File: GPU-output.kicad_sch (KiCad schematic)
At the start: 20 parts, among them J1 Conn_1-2212115-4, Q1 2N7002K-T1-E3, U4 TMCS1100A2-Q1

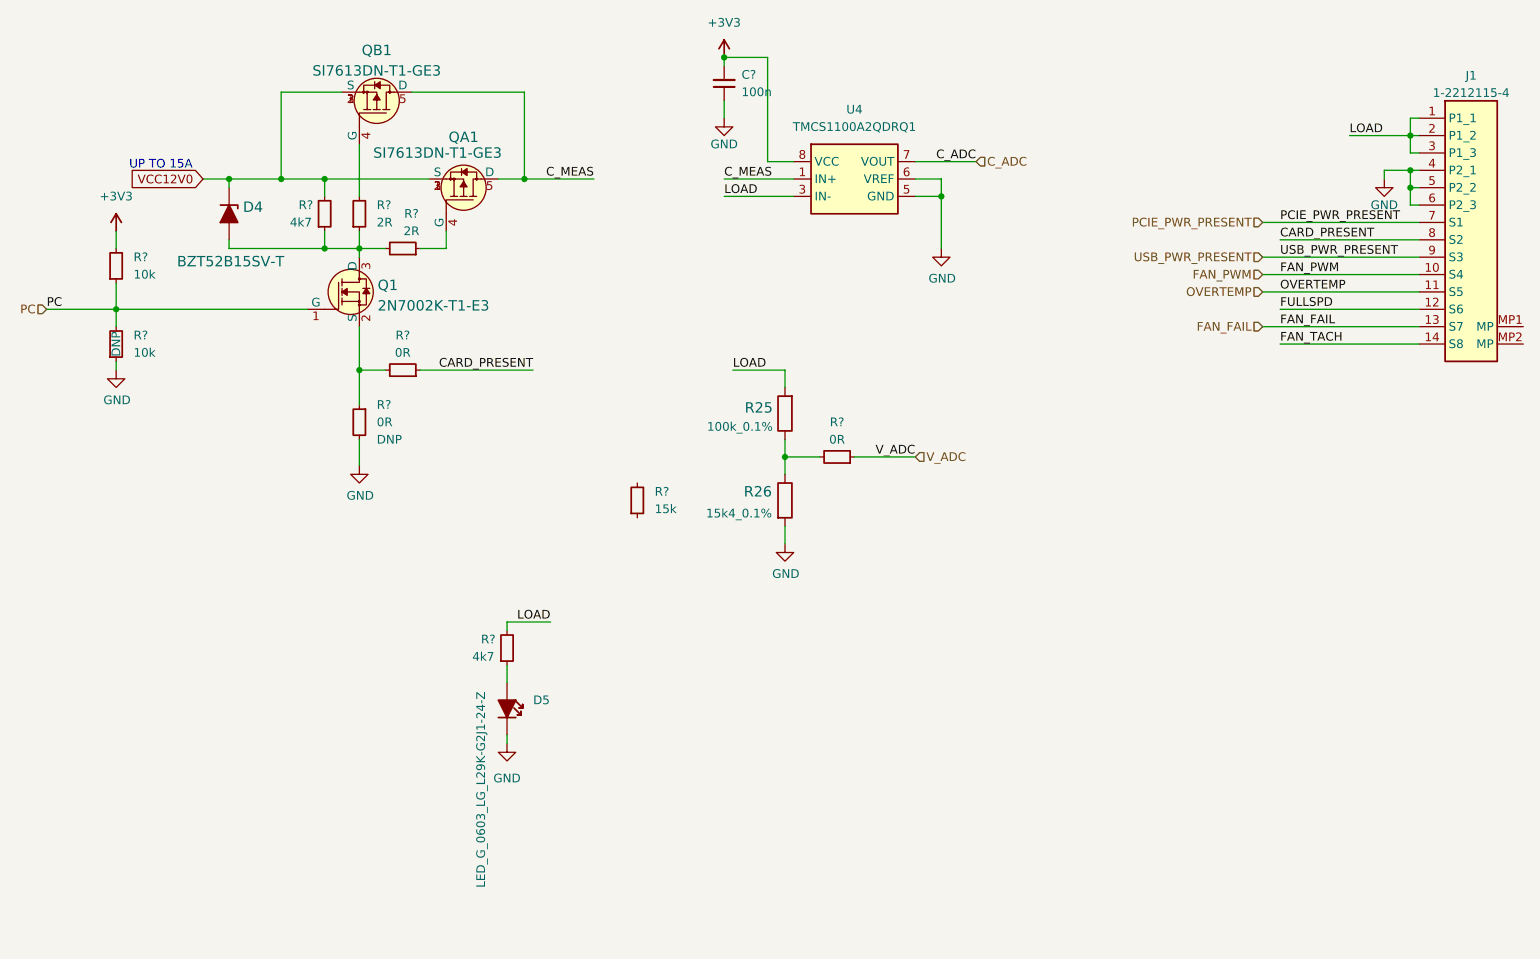
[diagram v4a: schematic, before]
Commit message: Standarize debug signal schematic
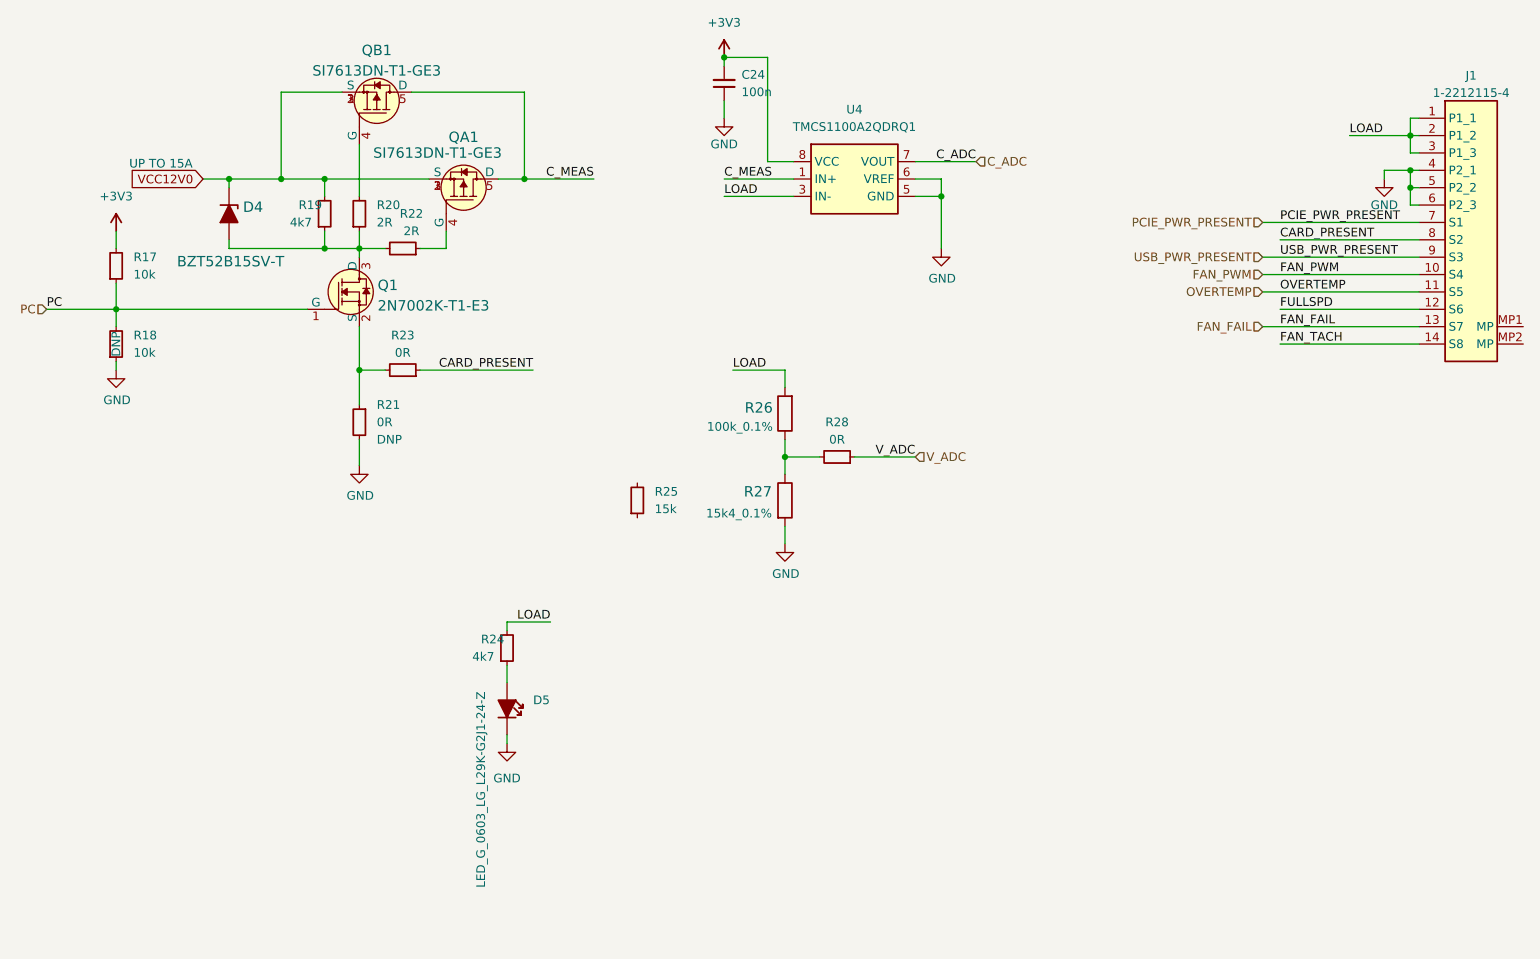
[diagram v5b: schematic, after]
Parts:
- gave numbers to parts that had none: 11
- renumbered R25 to R26, R26 to R27
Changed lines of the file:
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@@
   (symbol (lib_id "antmicroResistors0402:R_100k_0.1%_0402") (at 140.97 87.63 90) (unit 1)
     (in_bom yes) (on_board yes) (fields_autoplaced)
-    (property "Reference" "R25" (id 0) (at 139.1921 86.7954 90)
+    (property "Reference" "R26" (id 0) (at 139.1921 86.7954 90)
       (effects (font (size 1.524 1.524)) (justify left))
     )
@@
   (symbol (lib_name "R_0R_0402_1") (lib_id "antmicroResistors0402:R_0R_0402") (at 87.63 81.28 180) (unit 1)
     (in_bom yes) (on_board yes)
-    (property "Reference" "R?" (id 0) (at 85.09 76.2 0)
+    (property "Reference" "R23" (id 0) (at 85.09 76.2 0)
       (effects (font (size 1.27 1.27) (thickness 0.15)))
     )
@@
   (symbol (lib_name "R_4k7_0402_1") (lib_id "antmicroResistors0402:R_4k7_0402") (at 100.33 124.46 90) (unit 1)
     (in_bom yes) (on_board yes)
-    (property "Reference" "R?" (id 0) (at 96.52 120.65 90)
+    (property "Reference" "R24" (id 0) (at 96.52 120.65 90)
       (effects (font (size 1.27 1.27) (thickness 0.15)) (justify right))
     )
@@
   (symbol (lib_id "antmicroResistors0402:R_15k4_0.1%_0402") (at 140.97 100.33 270) (unit 1)
     (in_bom yes) (on_board yes)
-    (property "Reference" "R26" (id 0) (at 139.065 99.0601 90)
+    (property "Reference" "R27" (id 0) (at 139.065 99.0601 90)
       (effects (font (size 1.524 1.524)) (justify right))
     )
@@
   (symbol (lib_name "R_10k_0402_1") (lib_id "antmicroResistors0402:R_10k_0402") (at 43.18 68.58 90) (unit 1)
     (in_bom yes) (on_board yes) (fields_autoplaced)
-    (property "Reference" "R?" (id 0) (at 45.72 64.7699 90)
+    (property "Reference" "R17" (id 0) (at 45.72 64.7699 90)
       (effects (font (size 1.27 1.27) (thickness 0.15)) (justify right))
     )
@@
   (symbol (lib_name "R_4k7_0402_1") (lib_id "antmicroResistors0402:R_4k7_0402") (at 73.66 60.96 90) (unit 1)
     (in_bom yes) (on_board yes)
-    (property "Reference" "R?" (id 0) (at 69.85 57.15 90)
+    (property "Reference" "R19" (id 0) (at 69.85 57.15 90)
       (effects (font (size 1.27 1.27) (thickness 0.15)) (justify right))
     )
@@
   (symbol (lib_name "R_0R_0402_1") (lib_id "antmicroResistors0402:R_0R_0402") (at 151.13 93.98 180) (unit 1)
     (in_bom yes) (on_board yes)
-    (property "Reference" "R?" (id 0) (at 148.59 88.9 0)
+    (property "Reference" "R28" (id 0) (at 148.59 88.9 0)
       (effects (font (size 1.27 1.27) (thickness 0.15)))
     )
@@
   (symbol (lib_name "R_10k_0402_1") (lib_id "antmicroResistors0402:R_10k_0402") (at 43.18 80.01 90) (unit 1)
     (in_bom yes) (on_board yes)
-    (property "Reference" "R?" (id 0) (at 45.72 76.1999 90)
+    (property "Reference" "R18" (id 0) (at 45.72 76.1999 90)
       (effects (font (size 1.27 1.27) (thickness 0.15)) (justify right))
     )
@@
   (symbol (lib_id "antmicroResistors0402:R_15k_0.1%_0402") (at 119.38 102.87 90) (unit 1)
     (in_bom yes) (on_board yes) (fields_autoplaced)
-    (property "Reference" "R?" (id 0) (at 121.92 99.0599 90)
+    (property "Reference" "R25" (id 0) (at 121.92 99.0599 90)
       (effects (font (size 1.27 1.27) (thickness 0.15)) (justify right))
     )
@@
   (symbol (lib_name "R_2R_0402_1") (lib_id "antmicroResistors0402:R_2R_0402") (at 87.63 63.5 180) (unit 1)
     (in_bom yes) (on_board yes)
-    (property "Reference" "R?" (id 0) (at 86.36 58.42 0)
+    (property "Reference" "R22" (id 0) (at 86.36 58.42 0)
       (effects (font (size 1.27 1.27) (thickness 0.15)))
     )
@@
   (symbol (lib_name "R_2R_0402_1") (lib_id "antmicroResistors0402:R_2R_0402") (at 78.74 60.96 90) (unit 1)
     (in_bom yes) (on_board yes) (fields_autoplaced)
-    (property "Reference" "R?" (id 0) (at 81.28 57.1499 90)
+    (property "Reference" "R20" (id 0) (at 81.28 57.1499 90)
       (effects (font (size 1.27 1.27) (thickness 0.15)) (justify right))
     )
@@
   (symbol (lib_name "R_0R_0402_1") (lib_id "antmicroResistors0402:R_0R_0402") (at 78.74 86.36 270) (unit 1)
     (in_bom yes) (on_board yes) (fields_autoplaced)
-    (property "Reference" "R?" (id 0) (at 81.28 86.3599 90)
+    (property "Reference" "R21" (id 0) (at 81.28 86.3599 90)
       (effects (font (size 1.27 1.27) (thickness 0.15)) (justify left))
     )
@@
   (symbol (lib_name "C_100n_0402_1") (lib_id "antmicroCapacitors0402:C_100n_0402") (at 132.08 41.91 90) (unit 1)
     (in_bom yes) (on_board yes) (fields_autoplaced)
-    (property "Reference" "C?" (id 0) (at 134.62 38.0935 90)
-      (effects (font (size 1.27 1.27) (thickness 0.15)) (justify right))
-    )
+    (property "Reference" "C24" (id 0) (at 134.62 38.0935 90)
+      (effects (font (size 1.27 1.27) (thickness 0.15)) (justify right))
+    )

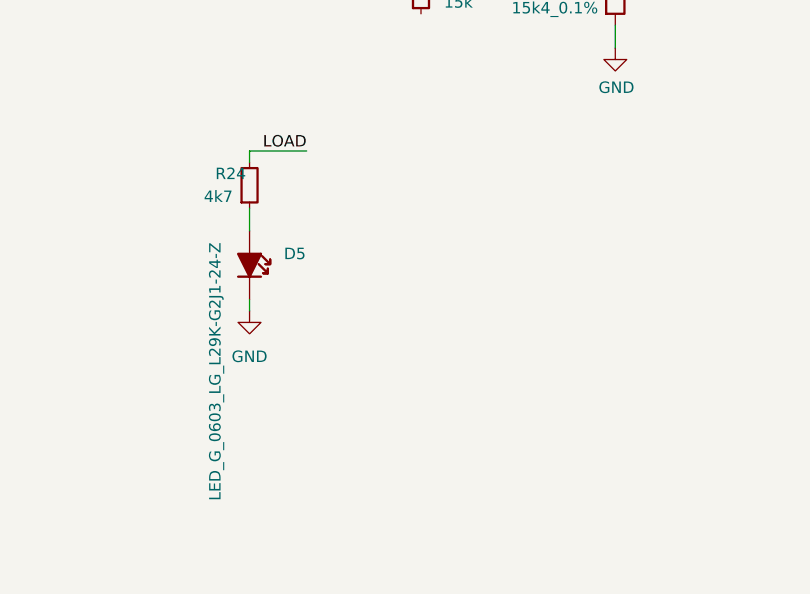
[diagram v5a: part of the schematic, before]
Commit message: Standarize missing components
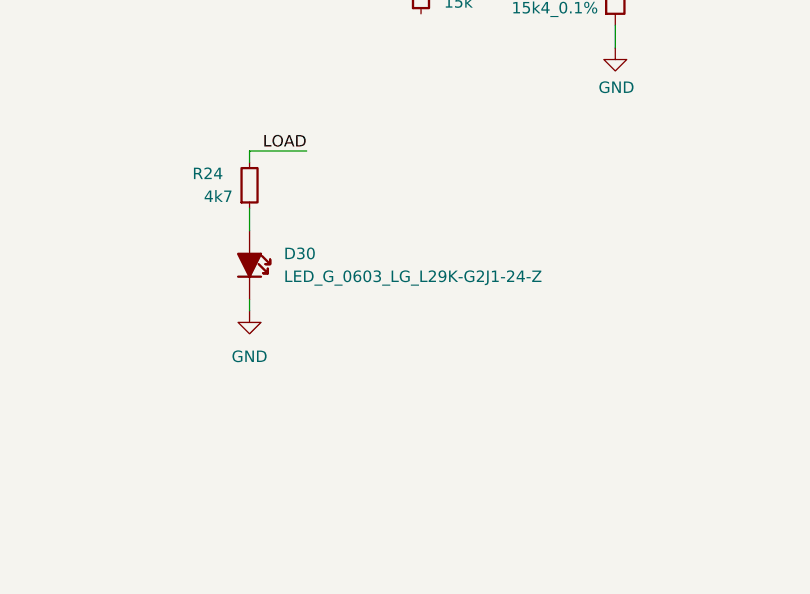
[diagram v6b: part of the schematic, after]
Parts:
- removed D5: LED_G_0603_LG_L29K-G2J1-24-Z, antmicro-footprints:LED_0603_1608Metric_G, symbol antmicroLEDIndicationDiscrete:LED_G_0603_LG_L29K-G2J1-24-Z
- added D30: LED_G_0603_LG_L29K-G2J1-24-Z, antmicro-footprints:LED_0603_1608Metric_G, symbol antmicroLEDIndicationDiscrete:LED_G_0603_LG_L29K-G2J1-24-Z
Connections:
- net GND: now also D30.2
- net at R24.1: now also D30.1
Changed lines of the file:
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@@
   (symbol (lib_name "R_4k7_0402_1") (lib_id "antmicroResistors0402:R_4k7_0402") (at 100.33 124.46 90) (unit 1)
     (in_bom yes) (on_board yes)
-    (property "Reference" "R24" (id 0) (at 96.52 120.65 90)
+    (property "Reference" "R24" (id 0) (at 93.98 120.65 90)
       (effects (font (size 1.27 1.27) (thickness 0.15)) (justify right))
     )
@@
     (pin "2")
   )
+  (symbol (lib_id "antmicroLEDIndicationDiscrete:LED_G_0603_LG_L29K-G2J1-24-Z") (at 100.33 127 270) (unit 1)
+    (in_bom yes) (on_board yes) (fields_autoplaced)
+    (property "Reference" "D30" (id 0) (at 104.14 129.5399 90)
+      (effects (font (size 1.27 1.27) (thickness 0.15)) (justify left))
+    )
+    (property "Value" "LED_G_0603_LG_L29K-G2J1-24-Z" (id 1) (at 104.14 132.0799 90)
+      (effects (font (size 1.27 1.27) (thickness 0.15)) (justify left))
+    )
+    (property "Footprint" "antmicro-footprints:LED_0603_1608Metric_G" (id 2) (at 90.17 149.86 0)
+      (effects (font (size 1.27 1.27) (thickness 0.15)) (justify left bottom) hide)
+    )
+    (property "Datasheet" "https://dammedia.osram.info/media/resource/hires/osram-dam-2493945/LG%20L29K.pdf" (id 3) (at 87.63 149.86 0)
+      (effects (font (size 1.27 1.27) (thickness 0.15)) (justify left bottom) hide)
+    )
+    (property "MPN" "LG L29K-G2J1-24-Z" (id 4) (at 85.09 149.86 0)
+      (effects (font (size 1.27 1.27) (thickness 0.15)) (justify left bottom) hide)
+    )
+    (property "Manufacturer" "OSRAM" (id 5) (at 82.55 149.86 0)
+      (effects (font (size 1.27 1.27) (thickness 0.15)) (justify left bottom) hide)
+    )
+    (property "Author" "Antmicro" (id 6) (at 80.01 149.86 0)
+      (effects (font (size 1.27 1.27) (thickness 0.15)) (justify left bottom) hide)
+    )
+    (property "License" "Apache-2.0" (id 7) (at 77.47 149.86 0)
+      (effects (font (size 1.27 1.27) (thickness 0.15)) (justify left bottom) hide)
+    )
+    (pin "1")
+    (pin "2")
+  )
   (symbol (lib_id "antmicropower:GND") (at 100.33 135.89 0) (unit 1)
     (in_bom yes) (on_board yes) (fields_autoplaced)
@@
     (pin "1")
   )
-  (symbol (lib_id "antmicroLEDIndicationDiscrete:LED_G_0603_LG_L29K-G2J1-24-Z") (at 100.33 127 270) (unit 1)
-    (in_bom yes) (on_board yes)
-    (property "Reference" "D5" (id 0) (at 104.14 129.5399 90)
-      (effects (font (size 1.27 1.27) (thickness 0.15)) (justify left))
-    )
-    (property "Value" "LED_G_0603_LG_L29K-G2J1-24-Z" (id 1) (at 96.52 128.27 0)
-      (effects (font (size 1.27 1.27) (thickness 0.15)) (justify left))
-    )
-    (property "Footprint" "antmicro-footprints:LED_0603_1608Metric_G" (id 2) (at 90.17 149.86 0)
-      (effects (font (size 1.27 1.27) (thickness 0.15)) (justify left bottom) hide)
-    )
-    (property "Datasheet" "https://dammedia.osram.info/media/resource/hires/osram-dam-2493945/LG%20L29K.pdf" (id 3) (at 87.63 149.86 0)
-      (effects (font (size 1.27 1.27) (thickness 0.15)) (justify left bottom) hide)
-    )
-    (property "MPN" "LG L29K-G2J1-24-Z" (id 4) (at 85.09 149.86 0)
-      (effects (font (size 1.27 1.27) (thickness 0.15)) (justify left bottom) hide)
-    )
-    (property "Manufacturer" "OSRAM" (id 5) (at 82.55 149.86 0)
-      (effects (font (size 1.27 1.27) (thickness 0.15)) (justify left bottom) hide)
-    )
-    (property "Author" "Antmicro" (id 6) (at 80.01 149.86 0)
-      (effects (font (size 1.27 1.27) (thickness 0.15)) (justify left bottom) hide)
-    )
-    (property "License" "Apache-2.0" (id 7) (at 77.47 149.86 0)
-      (effects (font (size 1.27 1.27) (thickness 0.15)) (justify left bottom) hide)
-    )
-    (pin "1")
-    (pin "2")
-  )
   (symbol (lib_id "antmicroPowerMeasurement:TMCS1100A2-Q1") (at 142.24 50.8 0) (unit 1)

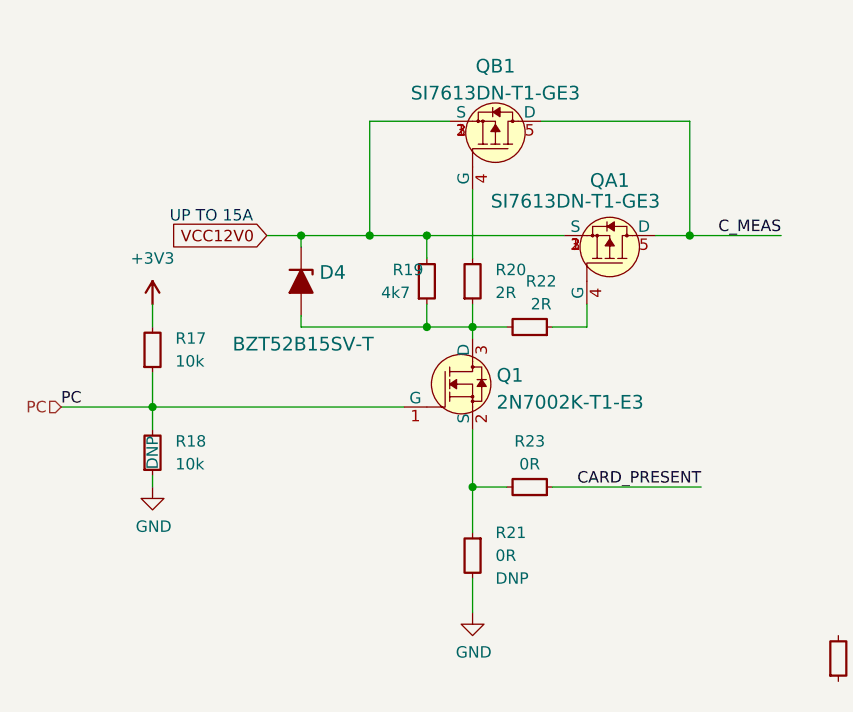
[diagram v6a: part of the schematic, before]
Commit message: 2nd batch of standardization of schematic
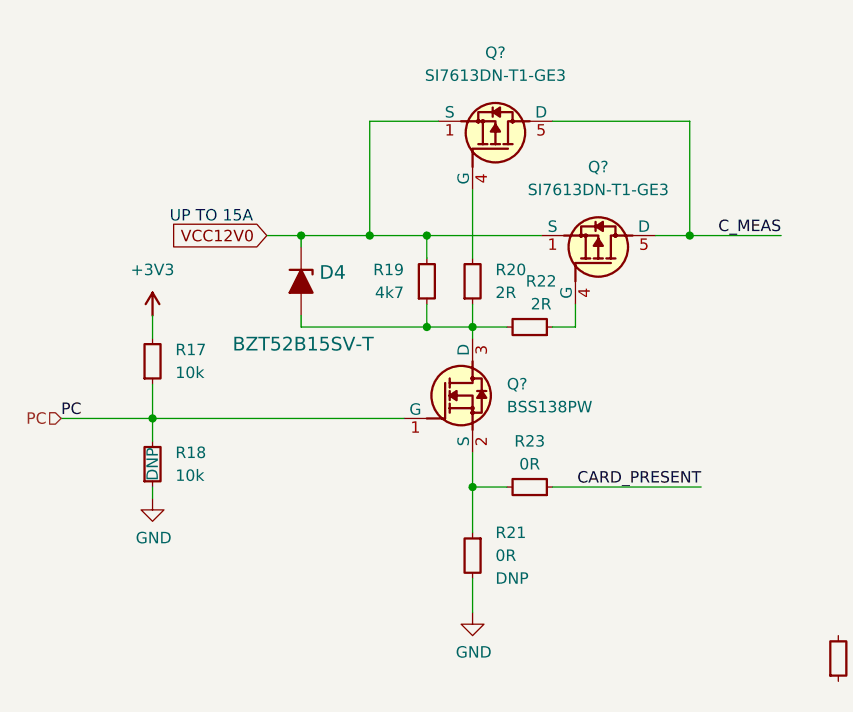
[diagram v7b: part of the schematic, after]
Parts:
- removed Q1: 2N7002K-T1-E3, antmicro-footprints:SOT-23-3, symbol antmicroTransistorsFETsMOSFETsSingle:2N7002K-T1-E3
- removed QA1, QB1: SI7613DN-T1-GE3, antmicro-footprints:Vishay_PowerPAK_1212-8_Single, symbol antmicroTransistorsFETsMOSFETsSingle:SI7613DN-T1-GE3
- added Q? (x2): SI7613DN-T1-GE3, antmicro-footprints:Vishay_PowerPAK_1212-8_Single, symbol antmicroTransistorsFETsMOSFETsSingle:SI7613DN-T1-GE3
- added Q?: BSS138PW, antmicro-footprints:SC70-3, symbol antmicroTransistorsFETsMOSFETsSingle:BSS138PW
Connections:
- net C_MEAS: now also Q?.5 (D), Q?.5 (D)
- net PC: now also Q?.1 (G)
- net VCC12V0: now also Q?.1 (S), Q?.1 (S), Q?.2 (S), Q?.2 (S), Q?.3 (S), Q?.3 (S)
- net at R21.1, R23.2: now also Q?.2 (S)
- net at D4.A, R19.1, R20.1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: now also Q?.3 (D)
- net at R22.1: now also Q?.4 (G)
- net at R20.2: now also Q?.4 (G)
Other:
- moved on the sheet: R17, R18

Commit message: Next batch of standardization
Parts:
- gave numbers to parts that had none: 3
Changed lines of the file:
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@@
   (symbol (lib_name "SI7613DN-T1-GE3_1") (lib_id "antmicroTransistorsFETsMOSFETsSingle:SI7613DN-T1-GE3") (at 78.74 48.26 270) (mirror x) (unit 1)
     (in_bom yes) (on_board yes) (fields_autoplaced)
-    (property "Reference" "Q?" (id 0) (at 81.28 33.02 90)
+    (property "Reference" "Q2" (id 0) (at 81.28 33.02 90)
       (effects (font (size 1.27 1.27) (thickness 0.15)))
     )
@@
   (symbol (lib_name "SI7613DN-T1-GE3_1") (lib_id "antmicroTransistorsFETsMOSFETsSingle:SI7613DN-T1-GE3") (at 90.17 60.96 270) (mirror x) (unit 1)
     (in_bom yes) (on_board yes) (fields_autoplaced)
-    (property "Reference" "Q?" (id 0) (at 92.71 45.72 90)
+    (property "Reference" "Q3" (id 0) (at 92.71 45.72 90)
       (effects (font (size 1.27 1.27) (thickness 0.15)))
     )
@@
   (symbol (lib_id "antmicroTransistorsFETsMOSFETsSingle:BSS138PW") (at 71.12 73.66 0) (unit 1)
     (in_bom yes) (on_board yes) (fields_autoplaced)
-    (property "Reference" "Q?" (id 0) (at 82.55 69.8499 0)
+    (property "Reference" "Q1" (id 0) (at 82.55 69.8499 0)
       (effects (font (size 1.27 1.27) (thickness 0.15)) (justify left))
     )
